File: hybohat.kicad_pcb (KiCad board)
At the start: 2 copper layers, 190.5 x 109.9 mm, 45 parts, among them J1 DC-PWR-IN, J2 IO_JACK_M03, J3 IO_JACK_M07, J4 IO_JACK_M03, J5 IO_JACK_M03, J6 CONN_1x8

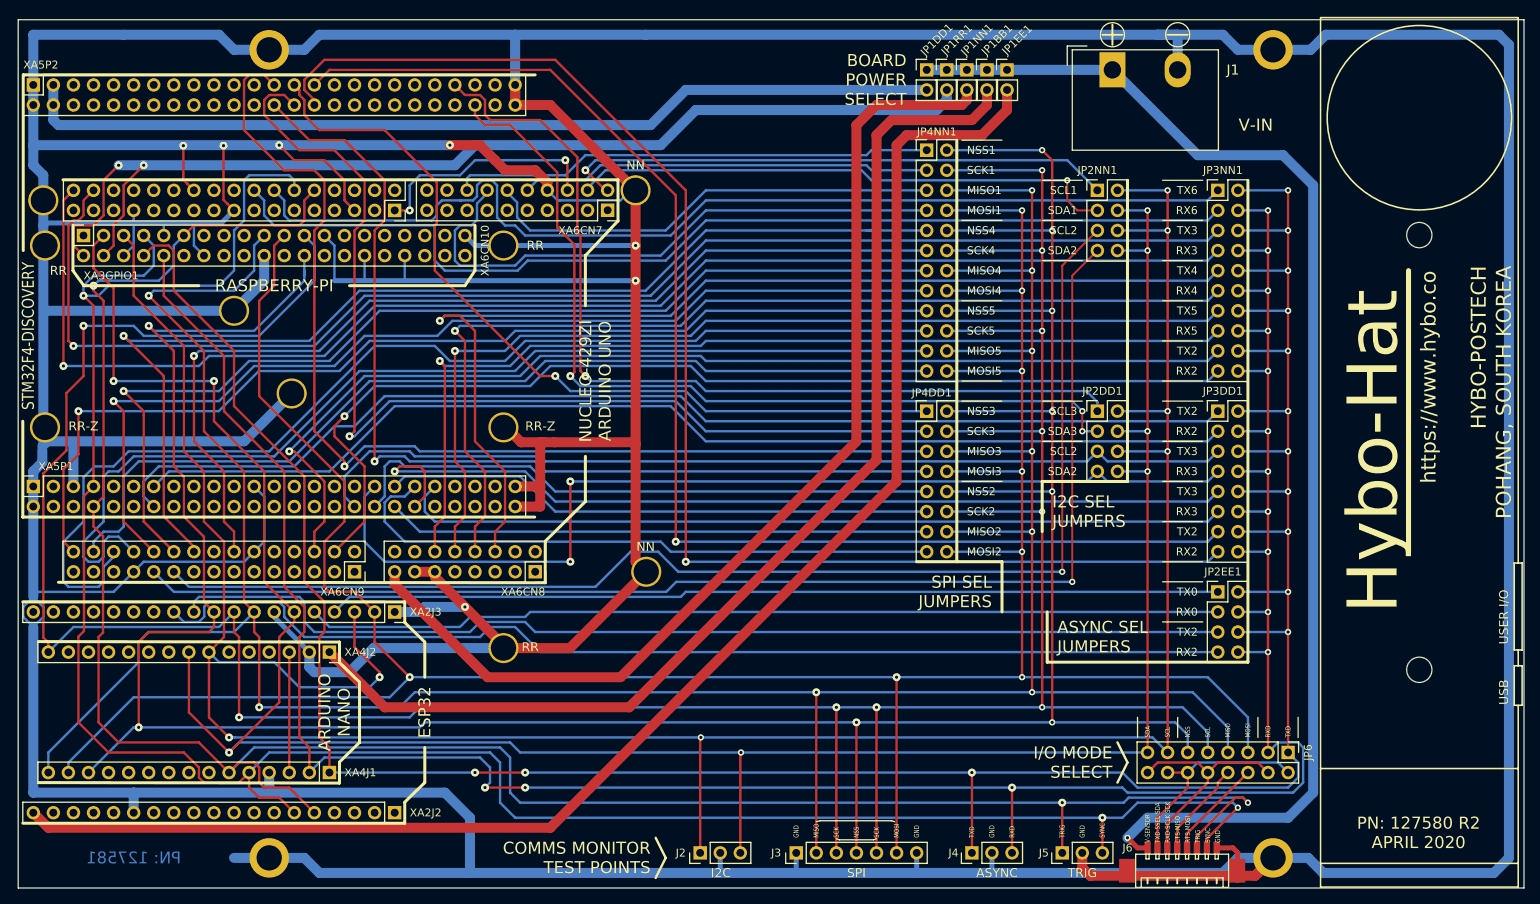
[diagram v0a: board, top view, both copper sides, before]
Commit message: updates for rev3, fixed Arduino Nano
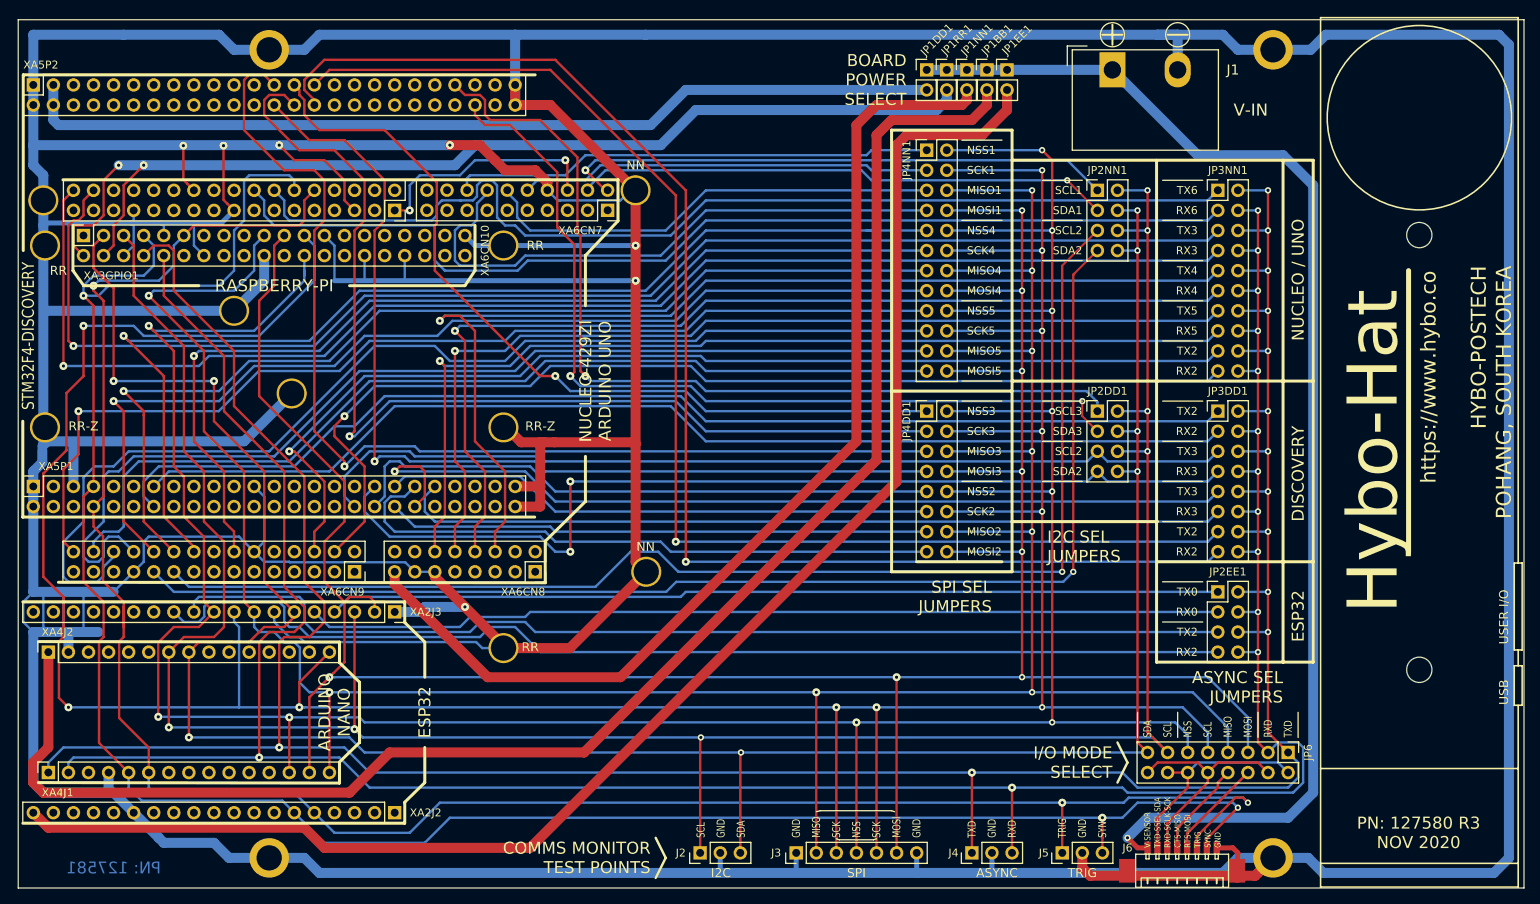
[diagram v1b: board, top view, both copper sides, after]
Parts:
- moved XA4J1 35.6 mm to (79.4, 127.0), turned to 90 degrees
- moved XA4J2 35.6 mm to (79.4, 111.8), turned to 90 degrees
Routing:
- net /BB_VIN: track 143.6 -> 200.5 mm
- net /BB_PB4_D12_MISO: track 381.1 -> 349.2 mm
- net /BB_PB3_D11_MOSI: track 359.5 -> 334.9 mm
- net /BB_PC5_D19_ADC5_A5_SCL: track 334.9 -> 317.3 mm
- net /ASYNC_RXD: track 333.3 -> 350.2 mm, vias 14 -> 13
- net /BB_PC6_RESET: track 15.2 -> 0.00 mm
- net /BB_PD3_D3_INT1: track 280.0 -> 266.5 mm
- net /ASYNC_TXD: track 358.0 -> 370.3 mm, vias 14 -> 13
- net /BB_PD2_D2_INT0: track 291.6 -> 279.5 mm
- net /BB_PB5_D13_SCK: track 413.7 -> 425.0 mm, vias 10 -> 11
- net /BB_PC4_D18_ADC4_A4_SDA: track 316.6 -> 306.9 mm
- net /BB_PB2_D10_NSS: track 388.4 -> 379.3 mm, vias 9 -> 10
- net GND: track 1208.9 -> 1214.1 mm
- net /DD_PB11_SDA2_RX3: track 128.3 -> 124.2 mm
- net /EE_EXT_5V: track 189.1 -> 191.2 mm
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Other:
- rule pad_to_mask_clearance: 0.051 -> 0
- board text added: "DISCOVERY"
- board text added: "NUCLEO / UNO"
- board text added: "PN: 127580 R3 NOV 2020"
- board text removed: "PN: 127580 R2 APRIL 2020"

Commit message: changed ESP32 module to have male pins
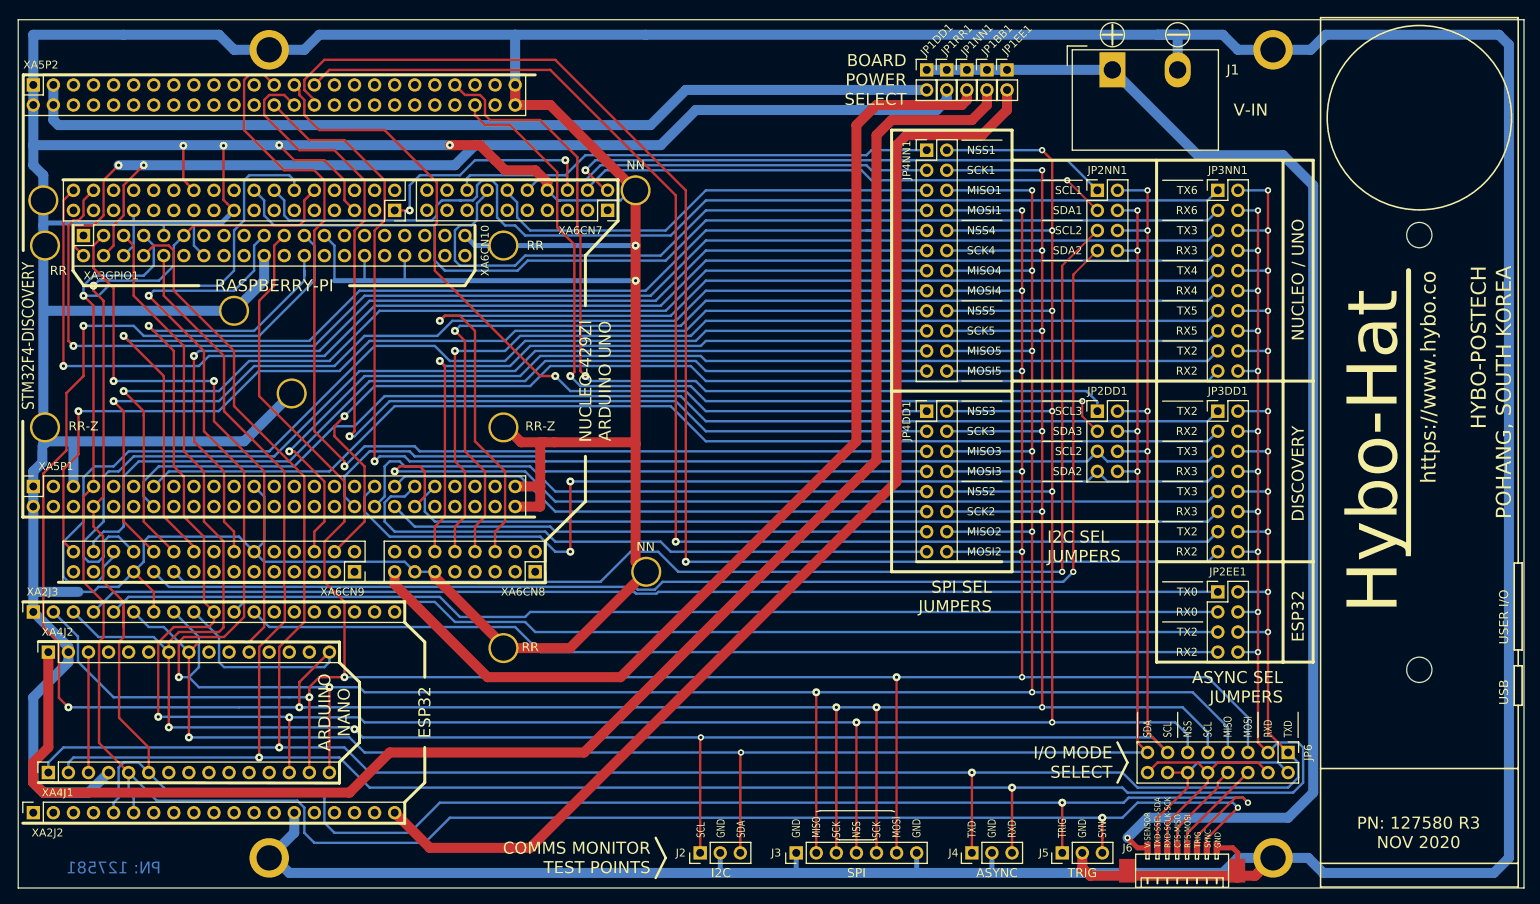
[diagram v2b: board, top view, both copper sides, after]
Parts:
- moved XA2J2 45.7 mm to (77.5, 132.1), turned to 90 degrees
- moved XA2J3 45.7 mm to (77.5, 106.7), turned to 90 degrees
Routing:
- net GND: track 1214.1 -> 1137.6 mm, vias 7 -> 6
- net /EE_EXT_5V: track 191.2 -> 145.4 mm
- net /BB_PB3_D11_MOSI: track 334.9 -> 368.0 mm, vias 8 -> 9
- net /EE_TXD0: track 112.8 -> 143.5 mm
- net /BB_PB4_D12_MISO: track 349.2 -> 376.5 mm, vias 9 -> 10
- net /EE_RXD0: track 115.9 -> 141.8 mm
- net /BB_PC6_RESET: track 0.00 -> 15.2 mm
- net /EE_IO16_RXD2: track 139.2 -> 124.0 mm
- net /BB_PD3_D3_INT1: track 266.5 -> 277.8 mm
- net /BB_PB5_D13_SCK: track 425.0 -> 435.7 mm
- net /EE_IO17_TXD2: track 135.5 -> 126.6 mm
- net /BB_PD2_D2_INT0: track 279.5 -> 285.6 mm
- net /BB_PC4_D18_ADC4_A4_SDA: track 306.9 -> 311.3 mm
- net /ASYNC_TXD: track 370.3 -> 366.4 mm
- net /ASYNC_RXD: track 350.2 -> 346.3 mm
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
